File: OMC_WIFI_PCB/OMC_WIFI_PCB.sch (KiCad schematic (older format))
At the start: 15 parts, among them J1 ESP32_Left, J10 Control_ACS712, J11 Control_ZMPT101B, J12 Power_Out_Load, J2 ESP32_Right, J3 Power_In, J4 Switch, J5 Pins_FT232R, J6 Line_Relay, J7 Control_Relay, J8 Line_ACS712, J9 Line_ZMPT101B

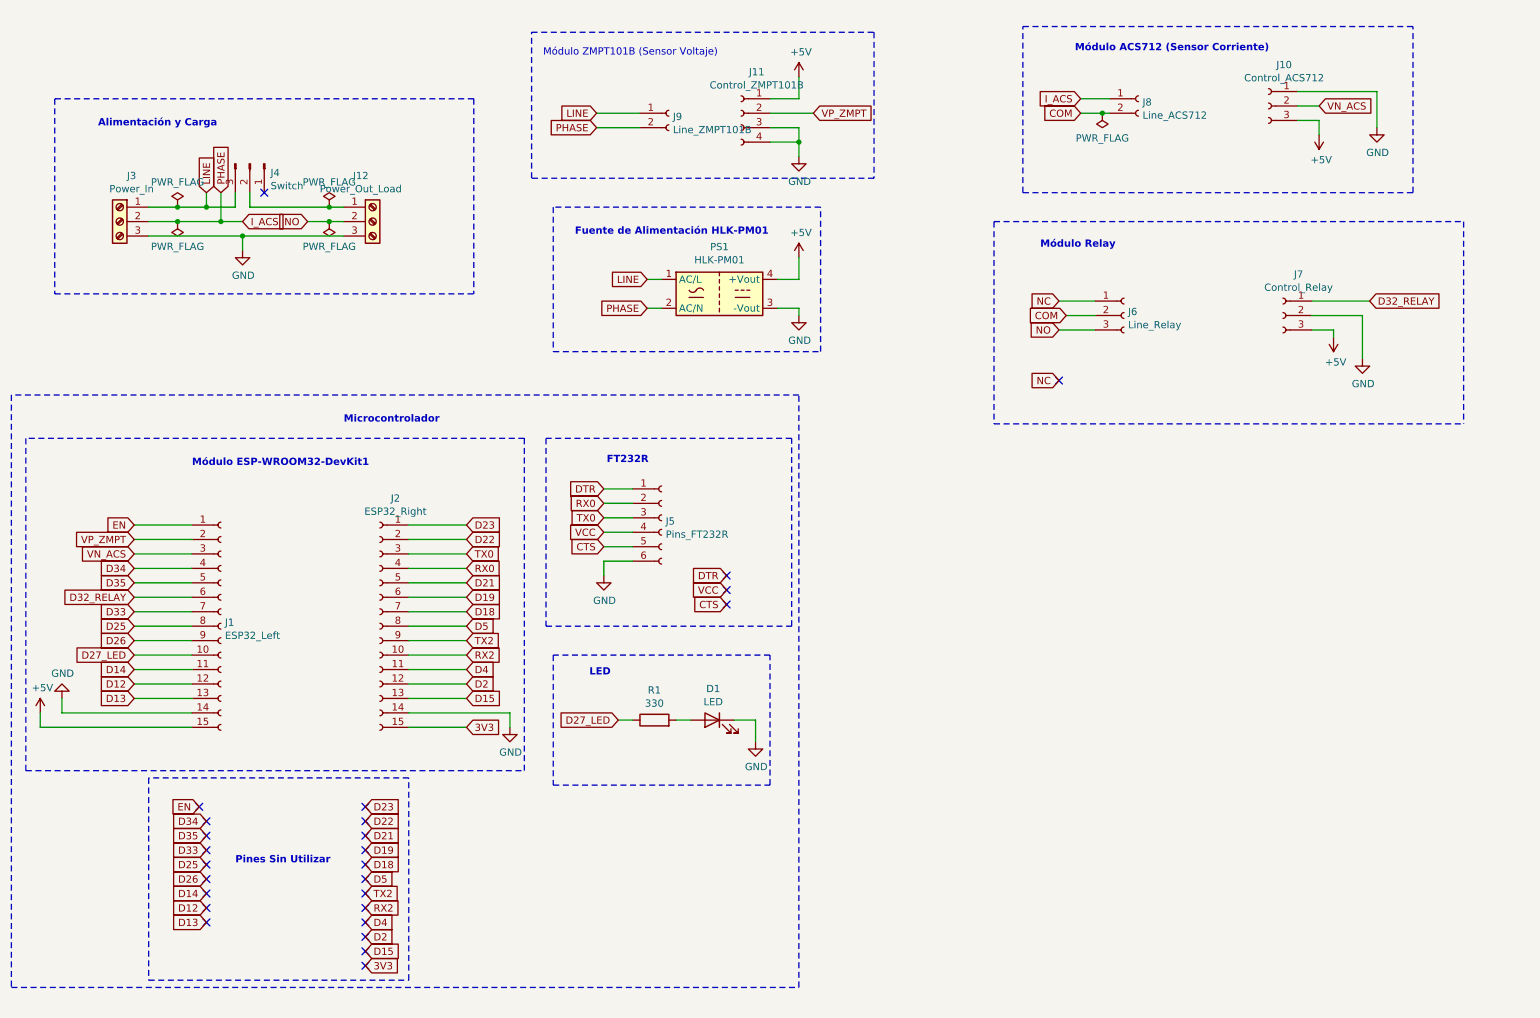
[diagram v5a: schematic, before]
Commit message: Actualización PCB
+ Pistas digitales
> Modificación de Tags
> Rediseño de la PCB
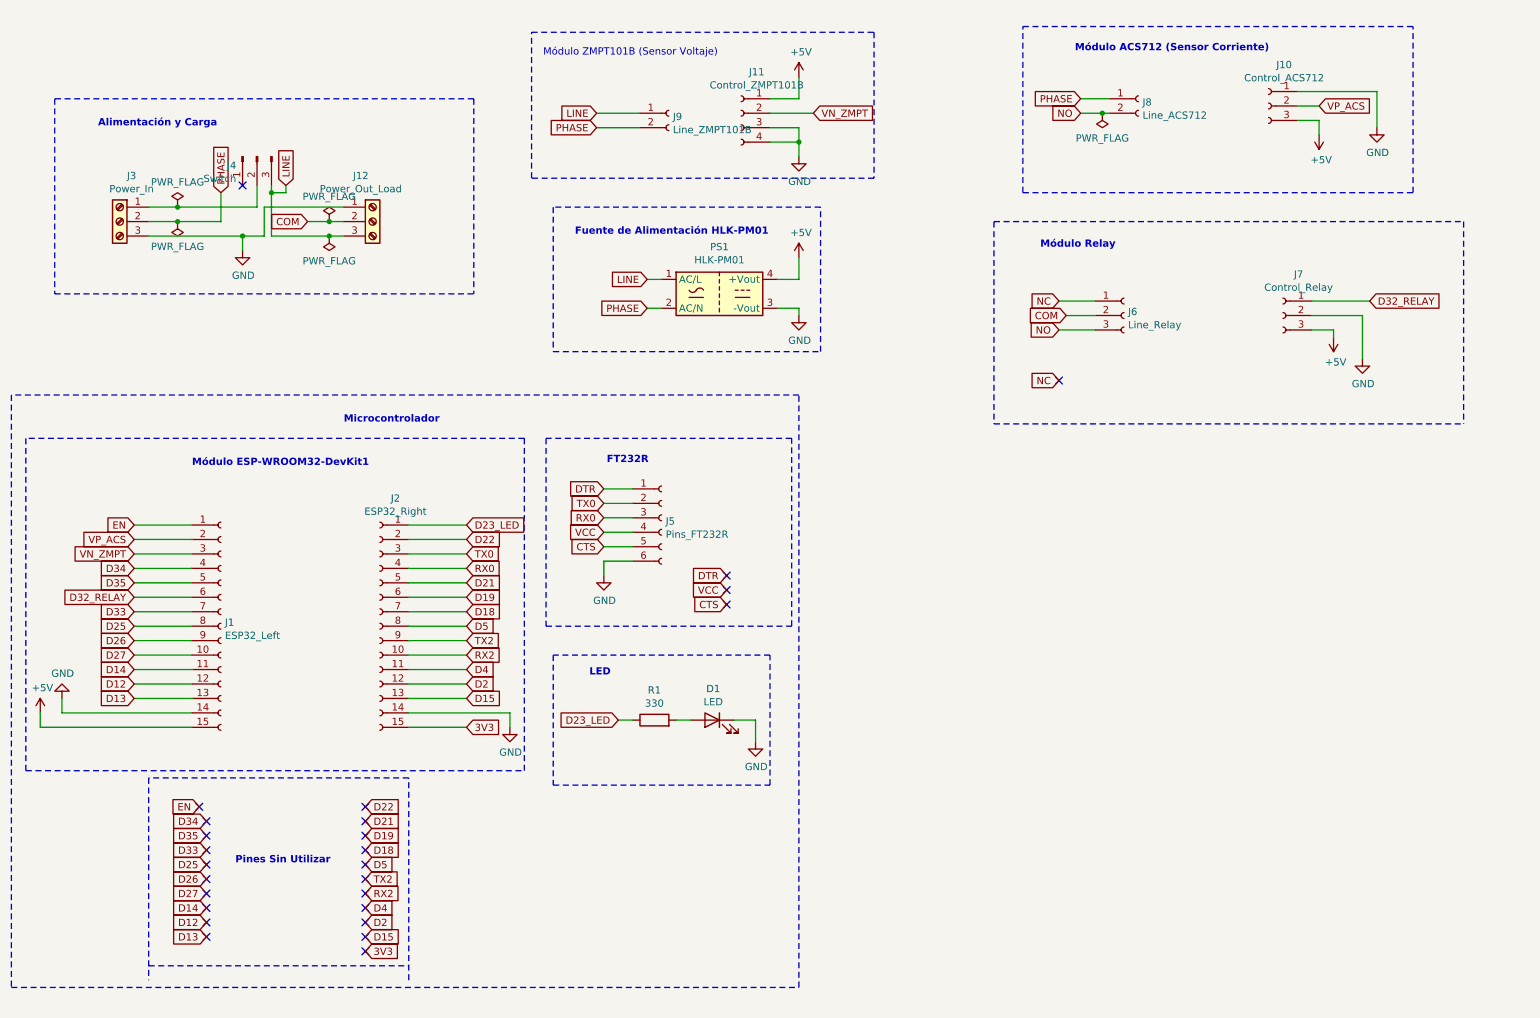
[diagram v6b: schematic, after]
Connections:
- net COM: now also J12.2 (Pin_2); no longer J8.2 (Pin_2)
- net GND: now also J12.1 (Pin_1); no longer J12.3 (Pin_3)
- net LINE: now also J12.3 (Pin_3); no longer J3.1 (Pin_1)
- net NO: now also J8.2 (Pin_2); no longer J12.2 (Pin_2)
- net RX0: now also J5.3 (Pin_3); no longer J5.2 (Pin_2)
- net TX0: now also J5.2 (Pin_2); no longer J5.3 (Pin_3)
- net at J4.2 (Pin_2): now also J3.1 (Pin_1); no longer J12.1 (Pin_1)
- net D23 renamed D23_LED
- net D23_LED: now also R1.1
- net D27_LED renamed D27
- net D27: no longer R1.1
- net I_ACS renamed PHASE
- net VN_ACS renamed VN_ZMPT
- net VN_ZMPT: now also J11.2 (Pin_2); no longer J10.2 (Pin_2)
- net VP_ZMPT renamed VP_ACS
- net VP_ACS: now also J10.2 (Pin_2); no longer J11.2 (Pin_2)
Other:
- moved on the sheet: J4
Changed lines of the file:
@@
 EN
 Text GLabel 1450 4250 0    50   Input ~ 0
-VP_ZMPT
+VP_ACS
 Text GLabel 1450 4350 0    50   Input ~ 0
-VN_ACS
+VN_ZMPT
 Text GLabel 1450 4450 0    50   Input ~ 0
 D34
@@
 D26
 Text GLabel 1450 5050 0    50   Input ~ 0
-D27_LED
+D27
 Text GLabel 1450 5150 0    50   Input ~ 0
 D14
@@
 D13
 Text GLabel 3750 4150 2    50   Input ~ 0
-D23
+D23_LED
 Text GLabel 3750 4250 2    50   Input ~ 0
 D22
@@
 	-1   0    0    -1
 $EndComp
-Text GLabel 2200 2050 2    50   Input ~ 0
-I_ACS
-Text GLabel 2650 2050 0    50   Input ~ 0
-NO
 Text GLabel 1900 6100 0    50   Input ~ 0
 EN
@@
 Text GLabel 1950 6600 0    50   Input ~ 0
 D26
-Text GLabel 1950 6700 0    50   Input ~ 0
+Text GLabel 1950 6800 0    50   Input ~ 0
 D14
-Text GLabel 1950 6800 0    50   Input ~ 0
+Text GLabel 1950 6900 0    50   Input ~ 0
 D12
-Text GLabel 1950 6900 0    50   Input ~ 0
+Text GLabel 1950 7000 0    50   Input ~ 0
 D13
 Text GLabel 3050 6100 2    50   Input ~ 0
-D23
+D22
 Text GLabel 3050 6200 2    50   Input ~ 0
-D22
+D21
 Text GLabel 3050 6300 2    50   Input ~ 0
-D21
+D19
 Text GLabel 3050 6400 2    50   Input ~ 0
-D19
+D18
 Text GLabel 3050 6500 2    50   Input ~ 0
-D18
+D5
 Text GLabel 3050 6600 2    50   Input ~ 0
-D5
+TX2
 Text GLabel 3050 6700 2    50   Input ~ 0
-TX2
+RX2
 Text GLabel 3050 6800 2    50   Input ~ 0
-RX2
+D4
 Text GLabel 3050 6900 2    50   Input ~ 0
-D4
+D2
 Text GLabel 3050 7000 2    50   Input ~ 0
-D2
+D15
 Text GLabel 3050 7100 2    50   Input ~ 0
-D15
-Text GLabel 3050 7200 2    50   Input ~ 0
 3V3
 NoConn ~ 1900 6100
@@
 NoConn ~ 1950 6500
 NoConn ~ 1950 6600
-NoConn ~ 1950 6700
 NoConn ~ 1950 6800
 NoConn ~ 1950 6900
+NoConn ~ 1950 7000
 NoConn ~ 3050 6100
 NoConn ~ 3050 6200
@@
 NoConn ~ 3050 7000
 NoConn ~ 3050 7100
-NoConn ~ 3050 7200
 Wire Wire Line
 	7850 2800 8100 2800
@@
 	5300 5500 5200 5500
 Text GLabel 4800 5500 0    50   Input ~ 0
-D27_LED
+D23_LED
 Wire Wire Line
 	4800 5500 4900 5500
@@
 NC
 NoConn ~ 7850 3150
-$Comp
-L Connector:Screw_Terminal_01x03 J12
-U 1 1 621955F9
-P 3100 2050
-F 0 "J12" H 3018 2367 50  0000 C CNN
-F 1 "Power_Out_Load" H 3018 2276 50  0000 C CNN
-F 2 "6PCV-03-006:TE_5-1437652-4" H 3100 2050 50  0001 C CNN
-F 3 "~" H 3100 2050 50  0001 C CNN
-	1    3100 2050
-	1    0    0    -1
-$EndComp
 $Comp
 L power:GND #PWR0117
@@
 Wire Wire Line
 	1550 2150 2200 2150
-Connection ~ 2200 2150
 Wire Wire Line
 	2200 2150 2200 2250
 Wire Wire Line
-	2200 2150 2900 2150
-Wire Wire Line
-	2150 1850 2150 1950
-Wire Wire Line
 	1550 1950 1750 1950
 Wire Wire Line
-	2250 1850 2250 1950
-Wire Wire Line
-	2250 1950 2800 1950
-Wire Wire Line
-	2200 2050 2050 2050
-Text GLabel 1950 1850 1    50   Input ~ 0
-LINE
-Text GLabel 2050 1850 1    50   Input ~ 0
-PHASE
-Wire Wire Line
-	1950 1850 1950 1950
-Connection ~ 1950 1950
-Wire Wire Line
-	1950 1950 2150 1950
-Wire Wire Line
 	2050 1850 2050 2050
-Connection ~ 2050 2050
 Wire Wire Line
 	2050 2050 1750 2050
@@
 $EndComp
 Text GLabel 4700 4100 0    50   Input ~ 0
+RX0
+Text GLabel 4700 4000 0    50   Input ~ 0
 TX0
-Text GLabel 4700 4000 0    50   Input ~ 0
-RX0
 Text Notes 4720 3730 0    50   ~ 10
 FT232R
@@
 	1550 5900 1550 7300
 Wire Notes Line
-	1550 7300 3350 7300
+	1550 7200 3350 7200
 Wire Notes Line
 	3350 7300 3350 5900
@@
 $EndComp
 Text GLabel 9650 1250 2    50   Input ~ 0
-VN_ACS
+VP_ACS
 $Comp
 L Connector:Conn_01x03_Female J10
@@
 	5850 1300 6150 1300
 Text GLabel 6150 1300 2    50   Input ~ 0
-VP_ZMPT
+VN_ZMPT
 Wire Wire Line
 	6050 1500 6050 1400
@@
 	1750 2050 1550 2050
 Connection ~ 1750 1950
-Wire Wire Line
-	1750 1950 1950 1950
-Wire Wire Line
-	2650 2050 2800 2050
-$Comp
-L power:PWR_FLAG #FLG0103
-U 1 1 624F2829
-P 2800 2050
-F 0 "#FLG0103" H 2800 2125 50  0001 C CNN
-F 1 "PWR_FLAG" H 2800 2223 50  0000 C CNN
-F 2 "" H 2800 2050 50  0001 C CNN
-F 3 "~" H 2800 2050 50  0001 C CNN
-	1    2800 2050
-	1    0    0    1
-$EndComp
-Connection ~ 2800 2050
-Wire Wire Line
-	2800 2050 2900 2050
-$Comp
-L power:PWR_FLAG #FLG0104
-U 1 1 624F3089
-P 2800 1950
-F 0 "#FLG0104" H 2800 2025 50  0001 C CNN
-F 1 "PWR_FLAG" H 2800 2123 50  0000 C CNN
-F 2 "" H 2800 1950 50  0001 C CNN
-F 3 "~" H 2800 1950 50  0001 C CNN
-	1    2800 1950
-	1    0    0    -1
-$EndComp
-Connection ~ 2800 1950
-Wire Wire Line
-	2800 1950 2900 1950
 Wire Notes Line
 	3800 1200 3800 2550
@@
 	1    0    0    1
 $EndComp
-Text GLabel 8000 1200 0    50   Input ~ 0
-I_ACS
 Text GLabel 8000 1300 0    50   Input ~ 0
-COM
+NO
 Wire Wire Line
 	8000 1300 8150 1300
@@
 Wire Notes Line
 	7400 3450 10650 3450
+NoConn ~ 2200 1800
+Text GLabel 8000 1200 0    50   Input ~ 0
+PHASE
+Text GLabel 2050 1850 1    50   Input ~ 0
+PHASE
+Text GLabel 2500 1800 1    50   Input ~ 0
+LINE
+Wire Wire Line
+	2300 1800 2300 1950
+Text GLabel 1950 6700 0    50   Input ~ 0
+D27
+NoConn ~ 1950 6700
+Wire Wire Line
+	2350 1950 2350 2150
+Wire Wire Line
+	2350 2150 2200 2150
+Connection ~ 2200 2150
+Wire Wire Line
+	2800 2150 2900 2150
+$Comp
+L power:PWR_FLAG #FLG0104
+U 1 1 624F3089
+P 2800 2150
+F 0 "#FLG0104" H 2800 2225 50  0001 C CNN
+F 1 "PWR_FLAG" H 2800 2323 50  0000 C CNN
+F 2 "" H 2800 2150 50  0001 C CNN
+F 3 "~" H 2800 2150 50  0001 C CNN
+	1    2800 2150
+	1    0    0    1
+$EndComp
+Wire Wire Line
+	2800 2050 2900 2050
+Connection ~ 2800 2050
+$Comp
+L power:PWR_FLAG #FLG0103
+U 1 1 624F2829
+P 2800 2050
+F 0 "#FLG0103" H 2800 2125 50  0001 C CNN
+F 1 "PWR_FLAG" H 2800 2223 50  0000 C CNN
+F 2 "" H 2800 2050 50  0001 C CNN
+F 3 "~" H 2800 2050 50  0001 C CNN
+	1    2800 2050
+	1    0    0    -1
+$EndComp
+Wire Wire Line
+	2650 2050 2800 2050
+$Comp
+L Connector:Screw_Terminal_01x03 J12
+U 1 1 621955F9
+P 3100 2050
+F 0 "J12" H 3018 2367 50  0000 C CNN
+F 1 "Power_Out_Load" H 3018 2276 50  0000 C CNN
+F 2 "6PCV-03-006:TE_5-1437652-4" H 3100 2050 50  0001 C CNN
+F 3 "~" H 3100 2050 50  0001 C CNN
+	1    3100 2050
+	1    0    0    -1
+$EndComp
+Connection ~ 2800 2150
+Wire Wire Line
+	2400 2150 2800 2150
+Wire Wire Line
+	2900 1950 2350 1950
+Text GLabel 2650 2050 0    50   Input ~ 0
+COM
 $Comp
 L Connector:Conn_01x03_Male J4
 U 1 1 6216C21C
-P 2250 1650
-F 0 "J4" V 2312 1794 50  0000 L CNN
-F 1 "Switch" V 2403 1794 50  0000 L CNN
-F 2 "Connector_Wire:SolderWire-0.75sqmm_1x03_P4.8mm_D1.25mm_OD2.3mm" H 2250 1650 50  0001 C CNN
-F 3 "~" H 2250 1650 50  0001 C CNN
-	1    2250 1650
-	0    1    1    0
-$EndComp
-NoConn ~ 2350 1850
+P 2300 1600
+F 0 "J4" V 2362 1744 50  0000 L CNN
+F 1 "Switch" V 2453 1744 50  0000 L CNN
+F 2 "Connector_Wire:SolderWire-0.75sqmm_1x03_P4.8mm_D1.25mm_OD2.3mm" H 2300 1600 50  0001 C CNN
+F 3 "~" H 2300 1600 50  0001 C CNN
+	1    2300 1600
+	0    -1   1    0
+$EndComp
+Wire Wire Line
+	2400 1800 2400 1850
+Wire Wire Line
+	1750 1950 2300 1950
+Wire Wire Line
+	2500 1800 2500 1850
+Wire Wire Line
+	2500 1850 2400 1850
+Connection ~ 2400 1850
+Wire Wire Line
+	2400 1850 2400 2150
 $EndSCHEMATC

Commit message: Actualización PCB
+Plano de Tierra
> Rediseño PCB para utilizar un solo conector
> Redistribución de pistas
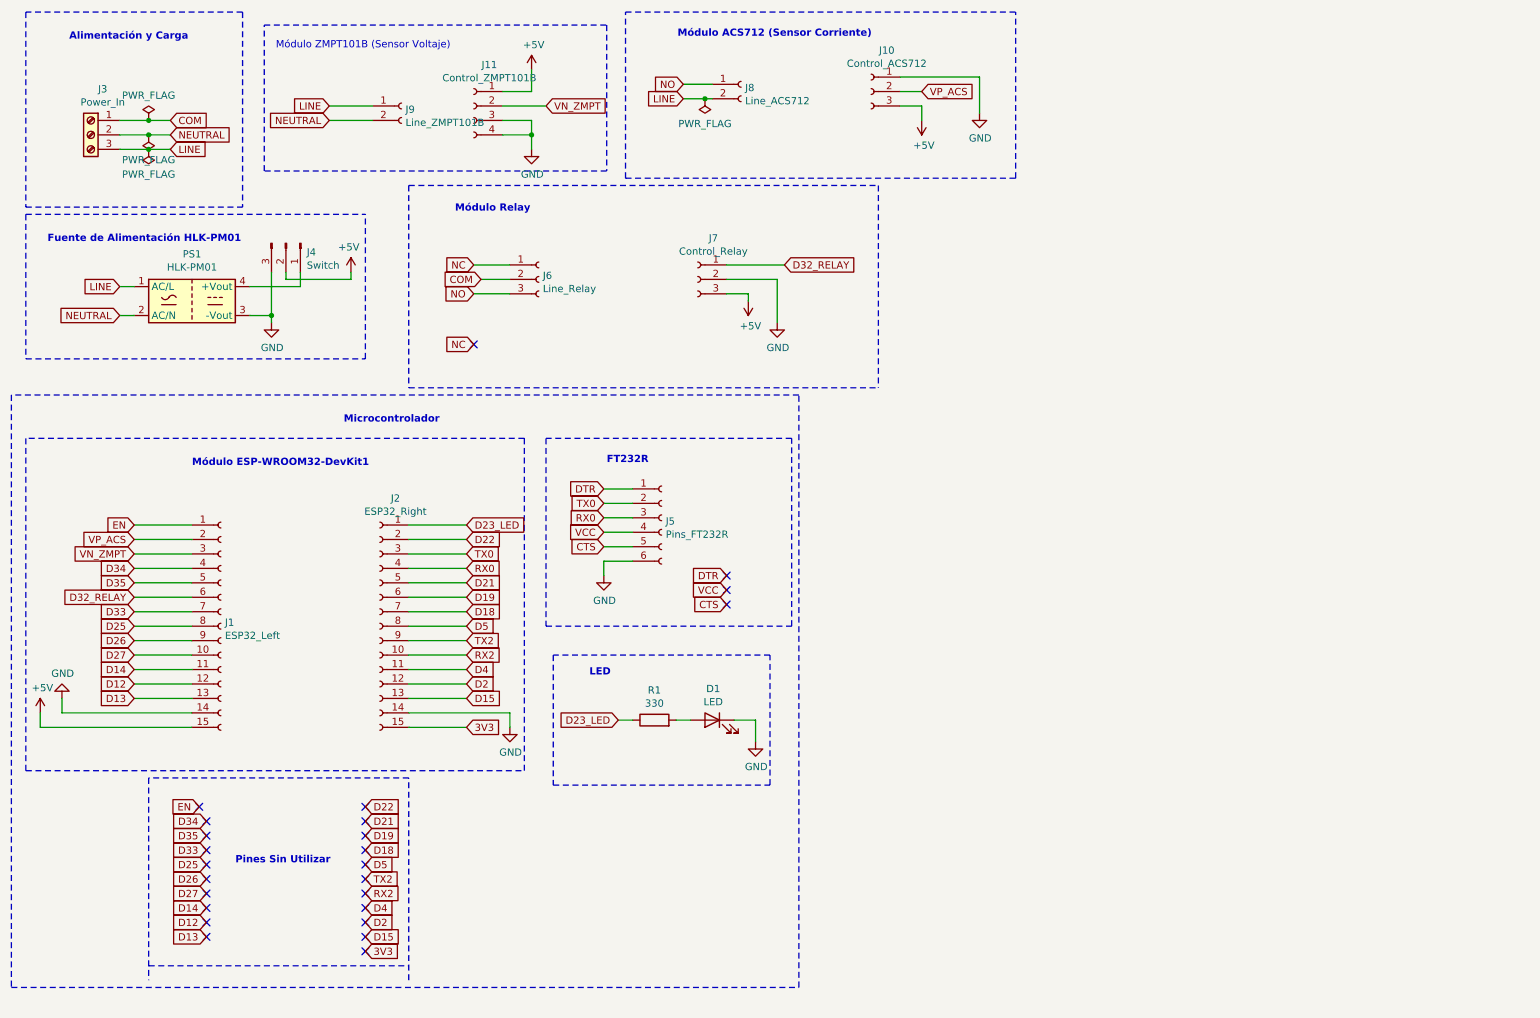
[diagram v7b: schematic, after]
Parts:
- removed J12: Power_Out_Load, 6PCV-03-006:TE_5-1437652-4, symbol Connector:Screw_Terminal_01x03
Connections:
- net +5V: now also J4.2 (Pin_2); no longer PS1.4 (+Vout)
- net COM: now also J3.1 (Pin_1)
- net GND: now also J4.3 (Pin_3); no longer J3.3 (Pin_3)
- net LINE: now also J3.3 (Pin_3), J8.2 (Pin_2); no longer J4.3 (Pin_3)
- net NO: now also J8.1 (Pin_1); no longer J8.2 (Pin_2)
- net at J4.1 (Pin_1): now also PS1.4 (+Vout)
- net PHASE renamed NEUTRAL
- net NEUTRAL: no longer J8.1 (Pin_1)
- no-connect marks 26 -> 25
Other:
- moved on the sheet: J10, J11, J3, J4, J6, J7, J8, J9, PS1
